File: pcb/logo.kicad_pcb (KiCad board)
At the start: 2 copper layers, 15.8 x 31.2 mm, 0 parts

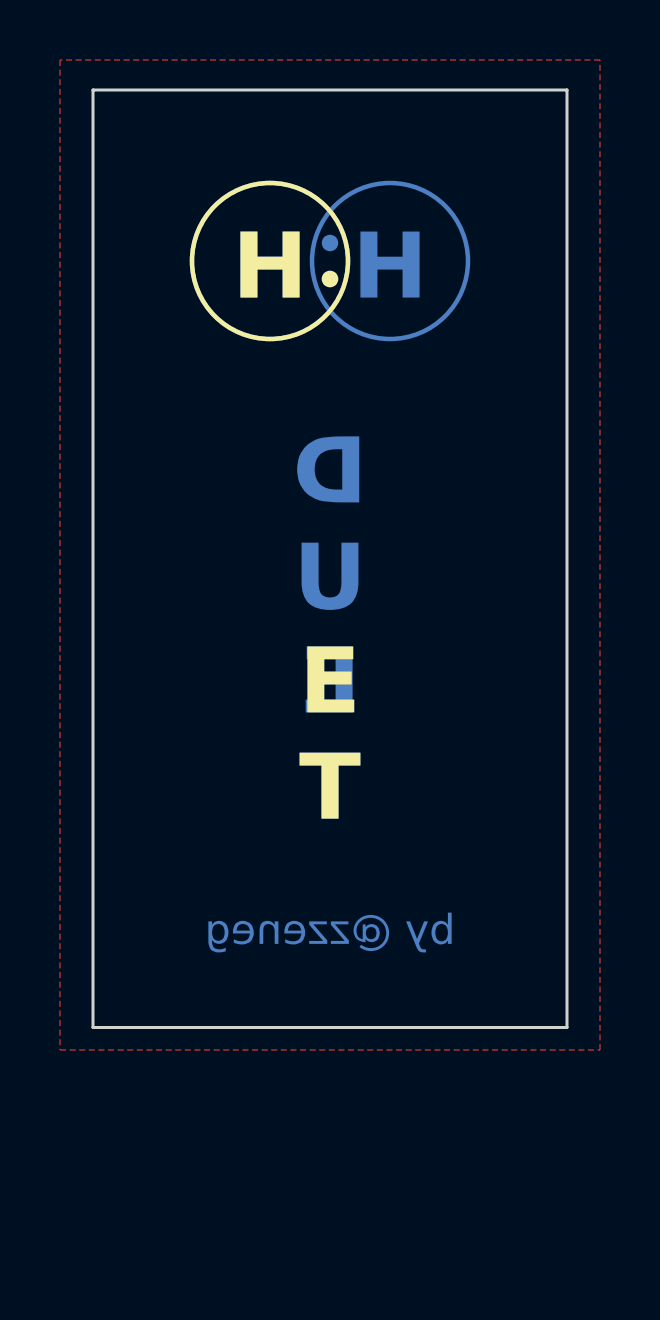
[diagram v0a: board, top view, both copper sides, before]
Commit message: small updates to silkscreen and logo
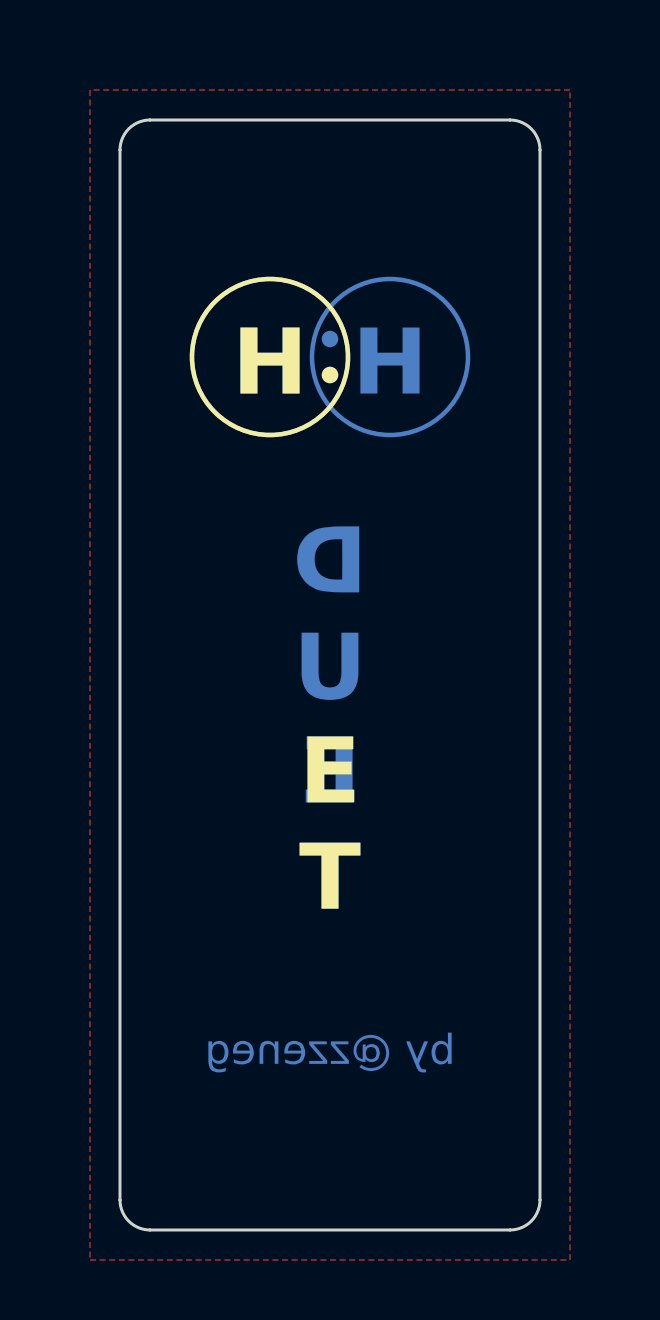
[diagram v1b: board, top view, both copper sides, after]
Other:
- board size 15.8 x 31.2 mm -> 14 x 37 mm

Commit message: add order number to logo
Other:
- board text added: "JLCJLCJLCJLC"
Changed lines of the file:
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@@
     )
+  )
+  (gr_text "JLCJLCJLCJLC" (at 86.9 85.5) (layer "B.SilkS")
+    (effects (font (size 0.8 0.8) (thickness 0.15)))
   )
   (gr_text "E\nT" (at 86.9 73.5) (layer "F.SilkS")
